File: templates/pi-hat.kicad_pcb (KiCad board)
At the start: 2 copper layers, 65 x 56 mm, 5 parts

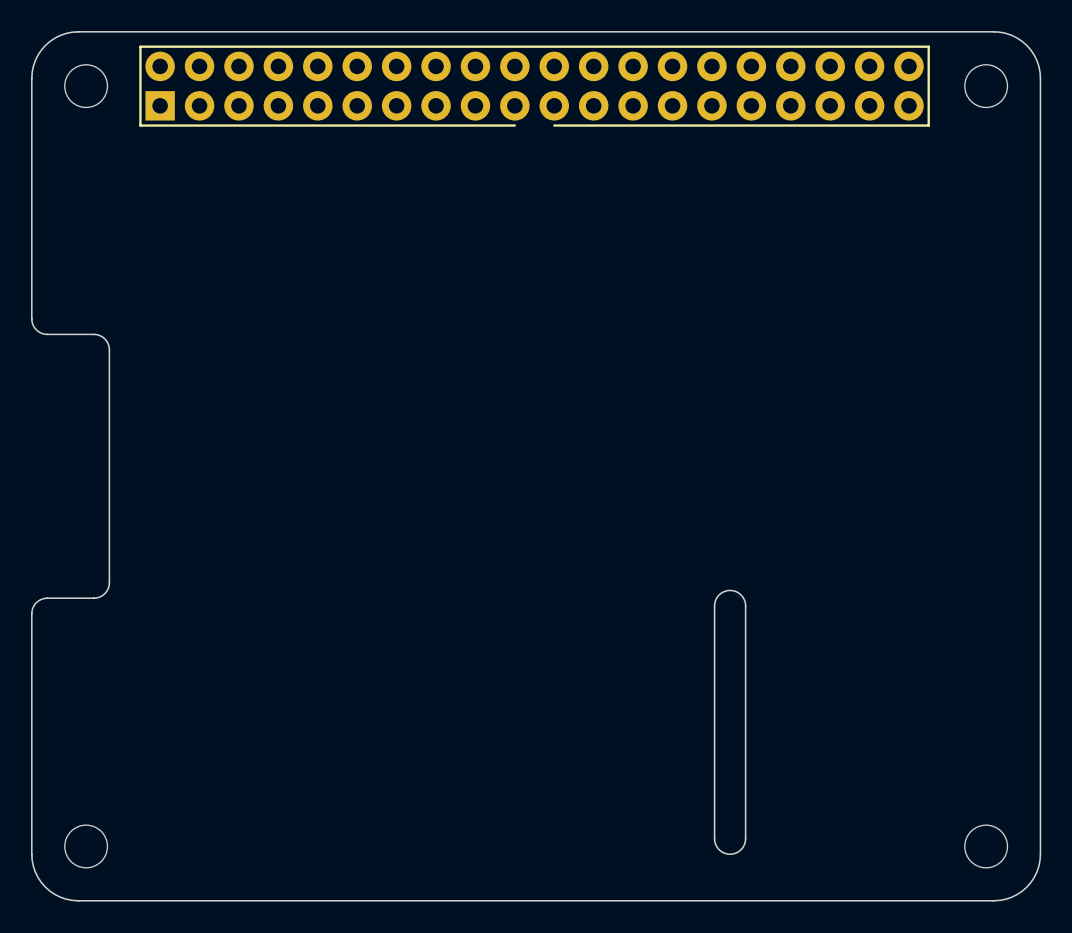
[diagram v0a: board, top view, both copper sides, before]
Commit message: Add M2.5_MOUNT and use it in the Pi templates
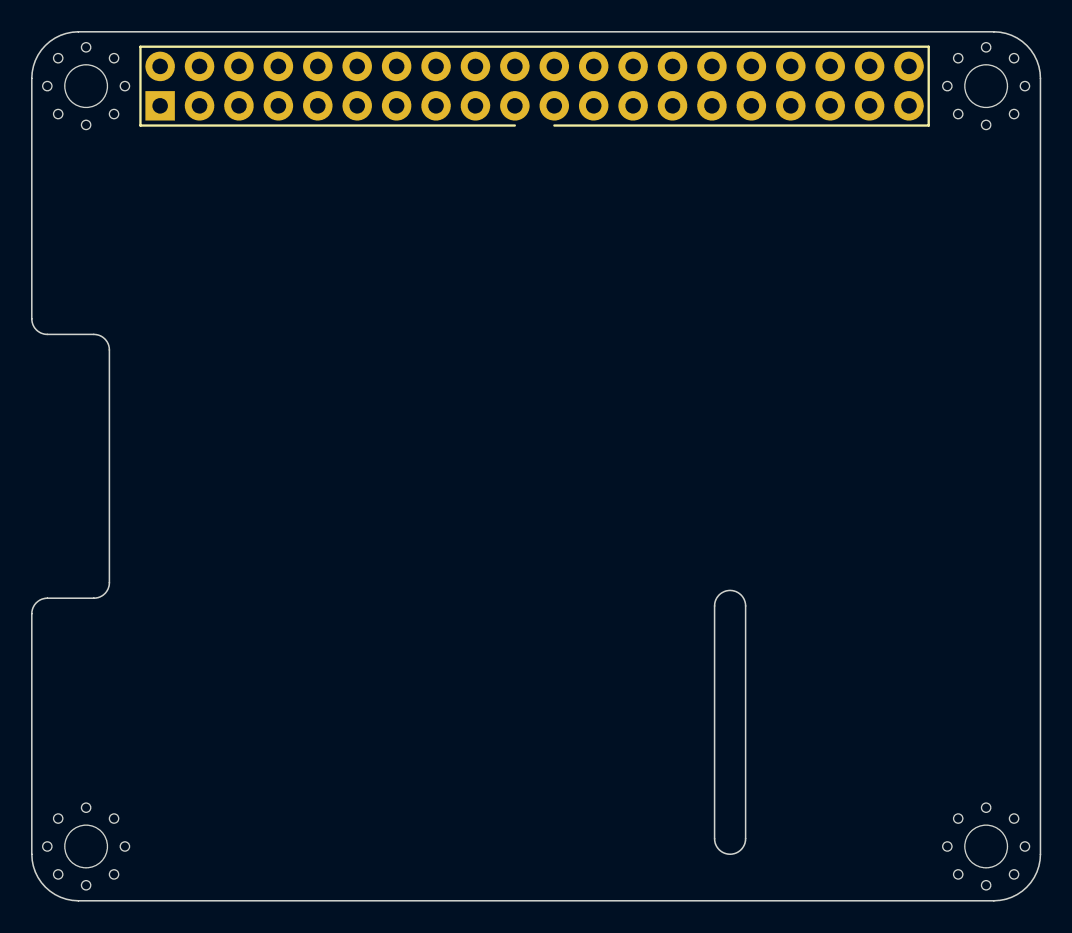
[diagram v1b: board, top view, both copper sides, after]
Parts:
- REF** (x4): value M2.5_HOLE -> M2.5_MOUNT; footprint agg:M2.5_HOLE -> agg:M2.5_MOUNT
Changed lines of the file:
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@@
     (links 0)
     (no_connects 0)
-    (area 110.177381 52.0525 176.822619 109.0925)
+    (area 109.558334 51.4425 177.441667 110.6925)
     (thickness 1.6)
     (drawings 20)
@@
     (uvia_drill 0.1)
   )
-  (module agg:M2.5_HOLE locked (layer F.Cu)
+  (module agg:M2.5_MOUNT locked (layer F.Cu)
     (at 172.5 105.5)
-    (solder_mask_margin 1.72)
-    (clearance 1.72)
-    (fp_text reference REF** (at 0 -2.5) (layer F.Fab) hide
+    (fp_text reference REF** (at 0 -4.1) (layer F.Fab) hide
       (effects (font (size 1 1) (thickness 0.15)))
     )
-    (fp_text value M2.5_HOLE (at 0 2.5) (layer F.Fab) hide
+    (fp_text value M2.5_MOUNT (at 0 4.1) (layer F.Fab) hide
       (effects (font (size 1 1) (thickness 0.15)))
     )
-    (fp_line (start -1.8 -1.8) (end 1.8 -1.8) (layer F.CrtYd) (width 0.01))
-    (fp_line (start 1.8 -1.8) (end 1.8 1.8) (layer F.CrtYd) (width 0.01))
-    (fp_line (start 1.8 1.8) (end -1.8 1.8) (layer F.CrtYd) (width 0.01))
-    (fp_line (start -1.8 1.8) (end -1.8 -1.8) (layer F.CrtYd) (width 0.01))
-    (pad "" np_thru_hole circle (at 0 0) (size 2.75 2.75) (drill 2.75) (layers *.Cu F.Mask))
+    (fp_line (start -3.4 -3.4) (end 3.4 -3.4) (layer F.CrtYd) (width 0.01))
+    (fp_line (start 3.4 -3.4) (end 3.4 3.4) (layer F.CrtYd) (width 0.01))
+    (fp_line (start 3.4 3.4) (end -3.4 3.4) (layer F.CrtYd) (width 0.01))
+    (fp_line (start -3.4 3.4) (end -3.4 -3.4) (layer F.CrtYd) (width 0.01))
+    (pad "" np_thru_hole circle (at 1.8 1.8) (size 0.6 0.6) (drill 0.6) (layers *.Cu *.Mask F.SilkS))
+    (pad "" np_thru_hole circle (at -1.8 1.8) (size 0.6 0.6) (drill 0.6) (layers *.Cu *.Mask F.SilkS))
+    (pad "" np_thru_hole circle (at 1.8 -1.8) (size 0.6 0.6) (drill 0.6) (layers *.Cu *.Mask F.SilkS))
+    (pad "" np_thru_hole circle (at -1.8 -1.8) (size 0.6 0.6) (drill 0.6) (layers *.Cu *.Mask F.SilkS))
+    (pad "" np_thru_hole circle (at -2.5 0) (size 0.6 0.6) (drill 0.6) (layers *.Cu *.Mask F.SilkS))
+    (pad "" np_thru_hole circle (at 0 2.5) (size 0.6 0.6) (drill 0.6) (layers *.Cu *.Mask F.SilkS))
+    (pad "" np_thru_hole circle (at 2.5 0) (size 0.6 0.6) (drill 0.6) (layers *.Cu *.Mask F.SilkS))
+    (pad "" np_thru_hole circle (at 0 -2.5) (size 0.6 0.6) (drill 0.6) (layers *.Cu *.Mask F.SilkS))
+    (pad "" np_thru_hole circle (at 0 0) (size 2.75 2.75) (drill 2.75) (layers *.Cu *.Mask F.SilkS)
+      (solder_mask_margin 1.72) (clearance 1.72))
   )
-  (module agg:M2.5_HOLE locked (layer F.Cu)
+  (module agg:M2.5_MOUNT locked (layer F.Cu)
     (at 114.5 105.5)
-    (solder_mask_margin 1.72)
-    (clearance 1.72)
-    (fp_text reference REF** (at 0 -2.5) (layer F.Fab) hide
+    (fp_text reference REF** (at 0 -4.1) (layer F.Fab) hide
       (effects (font (size 1 1) (thickness 0.15)))
     )
-    (fp_text value M2.5_HOLE (at 0 2.5) (layer F.Fab) hide
+    (fp_text value M2.5_MOUNT (at 0 4.1) (layer F.Fab) hide
       (effects (font (size 1 1) (thickness 0.15)))
     )
-    (fp_line (start -1.8 -1.8) (end 1.8 -1.8) (layer F.CrtYd) (width 0.01))
-    (fp_line (start 1.8 -1.8) (end 1.8 1.8) (layer F.CrtYd) (width 0.01))
-    (fp_line (start 1.8 1.8) (end -1.8 1.8) (layer F.CrtYd) (width 0.01))
-    (fp_line (start -1.8 1.8) (end -1.8 -1.8) (layer F.CrtYd) (width 0.01))
-    (pad "" np_thru_hole circle (at 0 0) (size 2.75 2.75) (drill 2.75) (layers *.Cu F.Mask))
+    (fp_line (start -3.4 -3.4) (end 3.4 -3.4) (layer F.CrtYd) (width 0.01))
+    (fp_line (start 3.4 -3.4) (end 3.4 3.4) (layer F.CrtYd) (width 0.01))
+    (fp_line (start 3.4 3.4) (end -3.4 3.4) (layer F.CrtYd) (width 0.01))
+    (fp_line (start -3.4 3.4) (end -3.4 -3.4) (layer F.CrtYd) (width 0.01))
+    (pad "" np_thru_hole circle (at 1.8 1.8) (size 0.6 0.6) (drill 0.6) (layers *.Cu *.Mask F.SilkS))
+    (pad "" np_thru_hole circle (at -1.8 1.8) (size 0.6 0.6) (drill 0.6) (layers *.Cu *.Mask F.SilkS))
+    (pad "" np_thru_hole circle (at 1.8 -1.8) (size 0.6 0.6) (drill 0.6) (layers *.Cu *.Mask F.SilkS))
+    (pad "" np_thru_hole circle (at -1.8 -1.8) (size 0.6 0.6) (drill 0.6) (layers *.Cu *.Mask F.SilkS))
+    (pad "" np_thru_hole circle (at -2.5 0) (size 0.6 0.6) (drill 0.6) (layers *.Cu *.Mask F.SilkS))
+    (pad "" np_thru_hole circle (at 0 2.5) (size 0.6 0.6) (drill 0.6) (layers *.Cu *.Mask F.SilkS))
+    (pad "" np_thru_hole circle (at 2.5 0) (size 0.6 0.6) (drill 0.6) (layers *.Cu *.Mask F.SilkS))
+    (pad "" np_thru_hole circle (at 0 -2.5) (size 0.6 0.6) (drill 0.6) (layers *.Cu *.Mask F.SilkS))
+    (pad "" np_thru_hole circle (at 0 0) (size 2.75 2.75) (drill 2.75) (layers *.Cu *.Mask F.SilkS)
+      (solder_mask_margin 1.72) (clearance 1.72))
   )
-  (module agg:M2.5_HOLE locked (layer F.Cu)
+  (module agg:M2.5_MOUNT locked (layer F.Cu)
     (at 114.5 56.5)
-    (solder_mask_margin 1.72)
-    (clearance 1.72)
-    (fp_text reference REF** (at 0 -2.5) (layer F.Fab) hide
+    (fp_text reference REF** (at 0 -4.1) (layer F.Fab) hide
       (effects (font (size 1 1) (thickness 0.15)))
     )
-    (fp_text value M2.5_HOLE (at 0 2.5) (layer F.Fab) hide
+    (fp_text value M2.5_MOUNT (at 0 4.1) (layer F.Fab) hide
       (effects (font (size 1 1) (thickness 0.15)))
     )
-    (fp_line (start -1.8 -1.8) (end 1.8 -1.8) (layer F.CrtYd) (width 0.01))
-    (fp_line (start 1.8 -1.8) (end 1.8 1.8) (layer F.CrtYd) (width 0.01))
-    (fp_line (start 1.8 1.8) (end -1.8 1.8) (layer F.CrtYd) (width 0.01))
-    (fp_line (start -1.8 1.8) (end -1.8 -1.8) (layer F.CrtYd) (width 0.01))
-    (pad "" np_thru_hole circle (at 0 0) (size 2.75 2.75) (drill 2.75) (layers *.Cu F.Mask))
+    (fp_line (start -3.4 -3.4) (end 3.4 -3.4) (layer F.CrtYd) (width 0.01))
+    (fp_line (start 3.4 -3.4) (end 3.4 3.4) (layer F.CrtYd) (width 0.01))
+    (fp_line (start 3.4 3.4) (end -3.4 3.4) (layer F.CrtYd) (width 0.01))
+    (fp_line (start -3.4 3.4) (end -3.4 -3.4) (layer F.CrtYd) (width 0.01))
+    (pad "" np_thru_hole circle (at 1.8 1.8) (size 0.6 0.6) (drill 0.6) (layers *.Cu *.Mask F.SilkS))
+    (pad "" np_thru_hole circle (at -1.8 1.8) (size 0.6 0.6) (drill 0.6) (layers *.Cu *.Mask F.SilkS))
+    (pad "" np_thru_hole circle (at 1.8 -1.8) (size 0.6 0.6) (drill 0.6) (layers *.Cu *.Mask F.SilkS))
+    (pad "" np_thru_hole circle (at -1.8 -1.8) (size 0.6 0.6) (drill 0.6) (layers *.Cu *.Mask F.SilkS))
+    (pad "" np_thru_hole circle (at -2.5 0) (size 0.6 0.6) (drill 0.6) (layers *.Cu *.Mask F.SilkS))
+    (pad "" np_thru_hole circle (at 0 2.5) (size 0.6 0.6) (drill 0.6) (layers *.Cu *.Mask F.SilkS))
+    (pad "" np_thru_hole circle (at 2.5 0) (size 0.6 0.6) (drill 0.6) (layers *.Cu *.Mask F.SilkS))
+    (pad "" np_thru_hole circle (at 0 -2.5) (size 0.6 0.6) (drill 0.6) (layers *.Cu *.Mask F.SilkS))
+    (pad "" np_thru_hole circle (at 0 0) (size 2.75 2.75) (drill 2.75) (layers *.Cu *.Mask F.SilkS)
+      (solder_mask_margin 1.72) (clearance 1.72))
   )
-  (module agg:M2.5_HOLE locked (layer F.Cu)
+  (module agg:M2.5_MOUNT locked (layer F.Cu)
     (at 172.5 56.5)
-    (solder_mask_margin 1.72)
-    (clearance 1.72)
-    (fp_text reference REF** (at 0 -2.5) (layer F.Fab) hide
+    (fp_text reference REF** (at 0 -4.1) (layer F.Fab) hide
       (effects (font (size 1 1) (thickness 0.15)))
     )
-    (fp_text value M2.5_HOLE (at 0 2.5) (layer F.Fab) hide
+    (fp_text value M2.5_MOUNT (at 0 4.1) (layer F.Fab) hide
       (effects (font (size 1 1) (thickness 0.15)))
     )
-    (fp_line (start -1.8 -1.8) (end 1.8 -1.8) (layer F.CrtYd) (width 0.01))
-    (fp_line (start 1.8 -1.8) (end 1.8 1.8) (layer F.CrtYd) (width 0.01))
-    (fp_line (start 1.8 1.8) (end -1.8 1.8) (layer F.CrtYd) (width 0.01))
-    (fp_line (start -1.8 1.8) (end -1.8 -1.8) (layer F.CrtYd) (width 0.01))
-    (pad "" np_thru_hole circle (at 0 0) (size 2.75 2.75) (drill 2.75) (layers *.Cu F.Mask))
+    (fp_line (start -3.4 -3.4) (end 3.4 -3.4) (layer F.CrtYd) (width 0.01))
+    (fp_line (start 3.4 -3.4) (end 3.4 3.4) (layer F.CrtYd) (width 0.01))
+    (fp_line (start 3.4 3.4) (end -3.4 3.4) (layer F.CrtYd) (width 0.01))
+    (fp_line (start -3.4 3.4) (end -3.4 -3.4) (layer F.CrtYd) (width 0.01))
+    (pad "" np_thru_hole circle (at 1.8 1.8) (size 0.6 0.6) (drill 0.6) (layers *.Cu *.Mask F.SilkS))
+    (pad "" np_thru_hole circle (at -1.8 1.8) (size 0.6 0.6) (drill 0.6) (layers *.Cu *.Mask F.SilkS))
+    (pad "" np_thru_hole circle (at 1.8 -1.8) (size 0.6 0.6) (drill 0.6) (layers *.Cu *.Mask F.SilkS))
+    (pad "" np_thru_hole circle (at -1.8 -1.8) (size 0.6 0.6) (drill 0.6) (layers *.Cu *.Mask F.SilkS))
+    (pad "" np_thru_hole circle (at -2.5 0) (size 0.6 0.6) (drill 0.6) (layers *.Cu *.Mask F.SilkS))
+    (pad "" np_thru_hole circle (at 0 2.5) (size 0.6 0.6) (drill 0.6) (layers *.Cu *.Mask F.SilkS))
+    (pad "" np_thru_hole circle (at 2.5 0) (size 0.6 0.6) (drill 0.6) (layers *.Cu *.Mask F.SilkS))
+    (pad "" np_thru_hole circle (at 0 -2.5) (size 0.6 0.6) (drill 0.6) (layers *.Cu *.Mask F.SilkS))
+    (pad "" np_thru_hole circle (at 0 0) (size 2.75 2.75) (drill 2.75) (layers *.Cu *.Mask F.SilkS)
+      (solder_mask_margin 1.72) (clearance 1.72))
   )
   (module agg:DIL-254P-40 locked (layer F.Cu)
